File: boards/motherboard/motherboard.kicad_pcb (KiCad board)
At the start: 2 copper layers, 36 parts, among them J1 RJ45, J2 RJ45, J3 RJ45, J4 RJ45, J5 RJ45, U1 EBAYPCA9685

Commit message: mother board pcb
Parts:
- added P1: CONN_01X02, Pin_Headers:Pin_Header_Straight_1x02, F.Cu at (74.9, 133.3)
- added P2: CONN_01X04, Pin_Headers:Pin_Header_Straight_1x04, F.Cu at (59.7, 129.5)
- added P3: CONN_01X04, Pin_Headers:Pin_Header_Straight_1x04, F.Cu at (59.7, 114.3)
- added REF**: MountingHole_2-5mm, Mounting_Holes:MountingHole_2-5mm, F.Cu at (91.4, 134.6)
- 350ma11, 350ma12, 350ma14, 350ma2, 350ma4, 350ma6, 350ma8: moved to B.Cu
- moved R3 146.2 mm to (238.8, 80.0)
- moved U1 139.8 mm to (256.5, 83.8), turned to 270 degrees
- moved J5 137.3 mm to (144.8, 130.8)
- moved R2 132.2 mm to (224.8, 80.0)
- moved R1 118.3 mm to (210.8, 80.0)
- moved J3 105.5 mm to (167.6, 130.8)
- moved R4 104.3 mm to (196.8, 80.0)
- moved 350ma12 97.9 mm to (146.2, 120.7), turned to 180 degrees
- moved R5 90.4 mm to (182.9, 80.0)
- moved 350ma14 89.5 mm to (98.4, 120.7), turned to 180 degrees
- moved 350ma15 77.1 mm to (66.9, 120.7)
- moved R6 76.4 mm to (168.9, 80.0)
- moved J4 68.8 mm to (190.5, 130.8)
- moved R8 62.5 mm to (154.9, 80.0)
- moved 350ma13 62.1 mm to (91.3, 120.7)
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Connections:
- 350ma9 pad 5: +24V -> /led8
- R12 pad 1: VCC -> Net-(R12-Pad1)
- R9 pad 2: +24V -> /led8
- U1 pad 19: Net-(U1-Pad19) -> /sda
- U1 pad 20: Net-(U1-Pad20) -> /scl
- U1 pad 9: +24V -> /led8
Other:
- board outline added: 223.5 x 63.5 mm
- net class 24vpower added: clearance 0.2, trace_width 2, via_dia 0.6, via_drill 0.4
- net class 350power added: clearance 0.2, trace_width 0.4, via_dia 0.6, via_drill 0.4

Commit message: sort of ok
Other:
- outline, holes or cut-outs redrawn
- net class 24vpower: trace_width 2 -> 8
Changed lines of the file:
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@@
   (net_class 24vpower ""
     (clearance 0.2)
-    (trace_width 2)
+    (trace_width 8)
     (via_dia 0.6)
     (via_drill 0.4)
@@
   (gr_line (start 53.34 139.7) (end 53.34 76.2) (angle 90) (layer Edge.Cuts) (width 0.15))
   (gr_line (start 276.86 139.7) (end 53.34 139.7) (angle 90) (layer Edge.Cuts) (width 0.15))
-  (gr_line (start 276.86 77.47) (end 276.86 139.7) (angle 90) (layer Edge.Cuts) (width 0.15))
+  (gr_line (start 276.86 76.2) (end 276.86 139.7) (angle 90) (layer Edge.Cuts) (width 0.15))
   (gr_line (start 276.86 76.2) (end 53.34 76.2) (angle 90) (layer Edge.Cuts) (width 0.15))
 )

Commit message: before autoroute
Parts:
- added REF10: MountingHole_2-5mm, Mounting_Holes:MountingHole_2-5mm, F.Cu at (251.5, 133.3)
- added REF2: MountingHole_2-5mm, Mounting_Holes:MountingHole_2-5mm, F.Cu at (58.7, 103.4)
- added REF3: MountingHole_2-5mm, Mounting_Holes:MountingHole_2-5mm, F.Cu at (251.5, 80.0)
- added REF4: MountingHole_2-5mm, Mounting_Holes:MountingHole_2-5mm, F.Cu at (121.9, 133.3)
- added REF5: MountingHole_2-5mm, Mounting_Holes:MountingHole_2-5mm, F.Cu at (146.1, 133.3)
- added REF6: MountingHole_2-5mm, Mounting_Holes:MountingHole_2-5mm, F.Cu at (168.9, 133.3)
- added REF7: MountingHole_2-5mm, Mounting_Holes:MountingHole_2-5mm, F.Cu at (191.8, 133.3)
- added REF8: MountingHole_2-5mm, Mounting_Holes:MountingHole_2-5mm, F.Cu at (214.6, 133.3)
- added REF9: MountingHole_2-5mm, Mounting_Holes:MountingHole_2-5mm, F.Cu at (237.5, 133.3)
- J1, J2, J3, J4, J5: footprint lighting:RJ45 -> Connect:RJ45_8
- P1: footprint Pin_Headers:Pin_Header_Straight_1x02 -> lighting:TerminalBlock
- moved P2 186.9 mm to (246.4, 138.4)
- moved P3 184.5 mm to (242.6, 138.4)
- moved P1 56.5 mm to (58.7, 79.2), turned to 180 degrees
- moved R14 46.0 mm to (86.4, 115.6)
- moved R1 29.2 mm to (210.8, 109.2)
- moved R10 29.2 mm to (85.1, 109.2)
- moved R11 29.2 mm to (99.1, 109.2)
- moved R12 29.2 mm to (127.0, 109.2)
- moved R13 29.2 mm to (71.1, 109.2)
- moved R2 29.2 mm to (224.8, 109.2)
- moved R3 29.2 mm to (238.8, 109.2)
- moved R4 29.2 mm to (196.8, 109.2)
- moved R5 29.2 mm to (182.9, 109.2)
- moved R6 29.2 mm to (168.9, 109.2)
- moved R7 29.2 mm to (113.0, 109.2)
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- renumbered REF** to REF1
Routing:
- net +24V: track 0.00 -> 355.8 mm
- net GNDPWR: track 0.00 -> 286.9 mm
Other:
- board size 223.5 x 63.5 mm -> 223.5 x 66 mm
- net class 24vpower: trace_width 8 -> 4

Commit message: after route
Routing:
- net VCC: track 0.00 -> 251.6 mm
- net GND: track 0.00 -> 251.5 mm
- net /led14: track 0.00 -> 222.7 mm
- net /led12: track 0.00 -> 203.3 mm
- net /led13: track 0.00 -> 192.5 mm
- net /led9: track 0.00 -> 180.1 mm
- net /led10: track 0.00 -> 166.1 mm
- net /led11: track 0.00 -> 147.3 mm
- net /led6: track 0.00 -> 145.8 mm
- net /led8: track 0.00 -> 128.4 mm
- net /led7: track 0.00 -> 111.8 mm
- net /led5: track 0.00 -> 95.3 mm
- net /led4: track 0.00 -> 95.3 mm
- net Net-(350ma15-Pad3): track 0.00 -> 71.7 mm
- net /led0: track 0.00 -> 69.0 mm
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
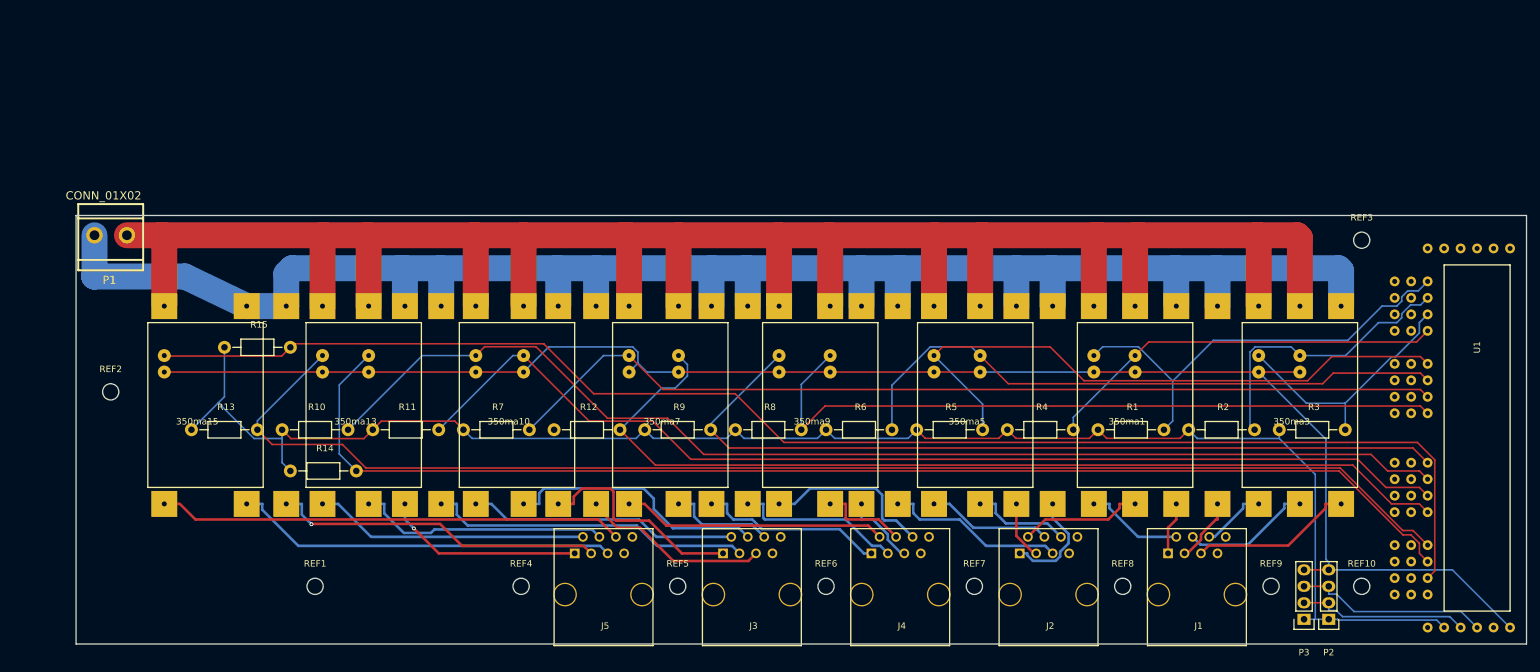
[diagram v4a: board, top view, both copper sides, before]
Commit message: moved parts around and swapped pca footprint
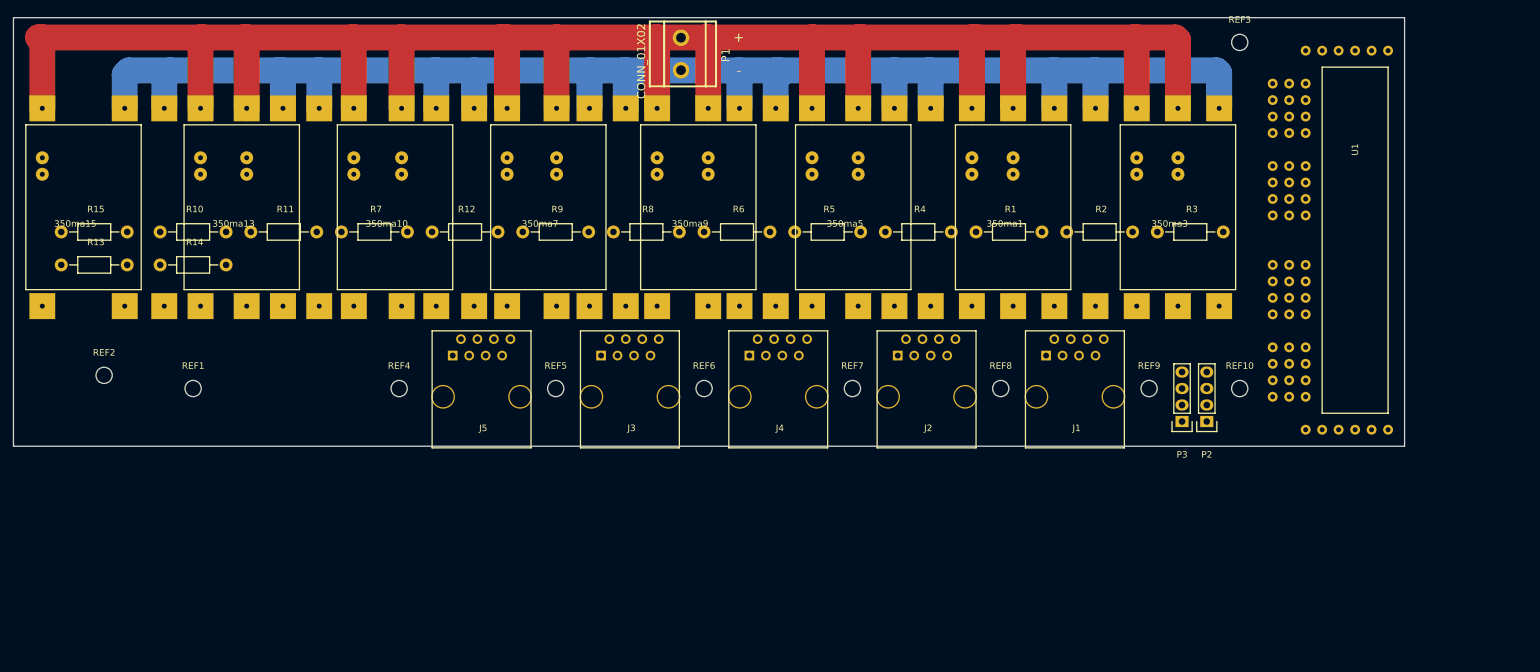
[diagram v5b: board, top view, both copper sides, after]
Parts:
- moved P1 92.2 mm to (146.6, 51.3), turned to 270 degrees
- moved R14 37.6 mm to (66.3, 83.8)
- moved 350ma3 35.8 mm to (216.8, 90.2)
- moved REF3 35.8 mm to (232.7, 49.5)
- moved U1 35.8 mm to (237.7, 55.9)
- moved 350ma10 35.8 mm to (96.1, 90.2)
- moved 350ma11 35.8 mm to (103.5, 90.2)
- moved 350ma13 35.8 mm to (72.5, 90.2)
- moved 350ma15 35.8 mm to (48.1, 90.2)
- moved J5 35.8 mm to (115.8, 104.1)
- moved R10 35.8 mm to (66.3, 78.7)
- moved R11 35.8 mm to (80.3, 78.7)
- moved R12 35.8 mm to (108.2, 78.7)
- moved R7 35.8 mm to (94.2, 78.7)
- moved 350ma1 35.8 mm to (191.4, 90.2)
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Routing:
- net VCC: track 251.6 -> 0.00 mm
- net GND: track 251.5 -> 0.00 mm
- net /led14: track 222.7 -> 0.00 mm
- net /led12: track 203.3 -> 0.00 mm
- net /led13: track 192.5 -> 0.00 mm
- net /led9: track 180.1 -> 0.00 mm
- net /led10: track 166.1 -> 0.00 mm
- net /led11: track 147.3 -> 0.00 mm
- net /led6: track 145.8 -> 0.00 mm
- net /led8: track 128.4 -> 0.00 mm
- net /led7: track 111.8 -> 0.00 mm
- net /led5: track 95.3 -> 0.00 mm
- net /led4: track 95.3 -> 0.00 mm
- net Net-(350ma15-Pad3): track 71.7 -> 0.00 mm
- net /led0: track 69.0 -> 0.00 mm
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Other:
- board size 223.5 x 66 mm -> 214.4 x 66 mm
- board text added: "+"
- board text added: "-"

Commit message: before auto route
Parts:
- moved REF1 51.3 mm to (54.6, 54.4)
- moved REF2 8.87 mm to (66.3, 102.9)
- moved REF3 3.05 mm to (235.7, 49.5)
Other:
- board text added: "This board can take up to 30V and drive 5 20W RGB LEDs. Do not use common anode or common cathode LEDs with this board."
- board text added: "gnd"
- board text added: "sda"
- board text added: "vcc"
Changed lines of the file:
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@@
     (area 43.612999 44.689419 258.139001 114.025)
     (thickness 1.6)
-    (drawings 6)
+    (drawings 13)
     (tracks 117)
     (zones 0)
@@
     (descr "Mounting hole, Befestigungsbohrung, 2,5mm, No Annular, Kein Restring,")
     (tags "Mounting hole, Befestigungsbohrung, 2,5mm, No Annular, Kein Restring,")
-    (fp_text reference REF10 (at 0 -3.50012) (layer F.SilkS)
+    (fp_text reference REF10 (at 0 -3.50012) (layer F.SilkS) hide
       (effects (font (size 1 1) (thickness 0.15)))
     )
@@
     (descr "Mounting hole, Befestigungsbohrung, 2,5mm, No Annular, Kein Restring,")
     (tags "Mounting hole, Befestigungsbohrung, 2,5mm, No Annular, Kein Restring,")
-    (fp_text reference REF9 (at 0 -3.50012) (layer F.SilkS)
+    (fp_text reference REF9 (at 0 -3.50012) (layer F.SilkS) hide
       (effects (font (size 1 1) (thickness 0.15)))
     )
@@
     (descr "Mounting hole, Befestigungsbohrung, 2,5mm, No Annular, Kein Restring,")
     (tags "Mounting hole, Befestigungsbohrung, 2,5mm, No Annular, Kein Restring,")
-    (fp_text reference REF8 (at 0 -3.50012) (layer F.SilkS)
+    (fp_text reference REF8 (at 0 -3.50012) (layer F.SilkS) hide
       (effects (font (size 1 1) (thickness 0.15)))
     )
@@
     (descr "Mounting hole, Befestigungsbohrung, 2,5mm, No Annular, Kein Restring,")
     (tags "Mounting hole, Befestigungsbohrung, 2,5mm, No Annular, Kein Restring,")
-    (fp_text reference REF7 (at 0 -3.50012) (layer F.SilkS)
+    (fp_text reference REF7 (at 0 -3.50012) (layer F.SilkS) hide
       (effects (font (size 1 1) (thickness 0.15)))
     )
@@
     (descr "Mounting hole, Befestigungsbohrung, 2,5mm, No Annular, Kein Restring,")
     (tags "Mounting hole, Befestigungsbohrung, 2,5mm, No Annular, Kein Restring,")
-    (fp_text reference REF6 (at 0 -3.50012) (layer F.SilkS)
+    (fp_text reference REF6 (at 0 -3.50012) (layer F.SilkS) hide
       (effects (font (size 1 1) (thickness 0.15)))
     )
@@
   )
   (module Mounting_Holes:MountingHole_2-5mm (layer F.Cu)
-    (at 232.664 49.53)
+    (at 235.712 49.53)
     (descr "Mounting hole, Befestigungsbohrung, 2,5mm, No Annular, Kein Restring,")
     (tags "Mounting hole, Befestigungsbohrung, 2,5mm, No Annular, Kein Restring,")
@@
   )
   (module Mounting_Holes:MountingHole_2-5mm (layer F.Cu)
-    (at 57.658 100.838)
+    (at 66.294 102.87)
     (descr "Mounting hole, Befestigungsbohrung, 2,5mm, No Annular, Kein Restring,")
     (tags "Mounting hole, Befestigungsbohrung, 2,5mm, No Annular, Kein Restring,")
-    (fp_text reference REF2 (at 0 -3.50012) (layer F.SilkS)
+    (fp_text reference REF2 (at 0 -3.50012) (layer F.SilkS) hide
       (effects (font (size 1 1) (thickness 0.15)))
     )
@@
   )
   (module Mounting_Holes:MountingHole_2-5mm (layer F.Cu)
-    (at 71.374 102.87)
+    (at 54.61 54.356)
     (descr "Mounting hole, Befestigungsbohrung, 2,5mm, No Annular, Kein Restring,")
     (tags "Mounting hole, Befestigungsbohrung, 2,5mm, No Annular, Kein Restring,")
-    (fp_text reference REF1 (at 0 -3.50012) (layer F.SilkS)
+    (fp_text reference REF1 (at 0 -3.50012) (layer F.SilkS) hide
       (effects (font (size 1 1) (thickness 0.15)))
     )
@@
     (descr "Mounting hole, Befestigungsbohrung, 2,5mm, No Annular, Kein Restring,")
     (tags "Mounting hole, Befestigungsbohrung, 2,5mm, No Annular, Kein Restring,")
-    (fp_text reference REF4 (at 0 -3.50012) (layer F.SilkS)
+    (fp_text reference REF4 (at 0 -3.50012) (layer F.SilkS) hide
       (effects (font (size 1 1) (thickness 0.15)))
     )
@@
     (descr "Mounting hole, Befestigungsbohrung, 2,5mm, No Annular, Kein Restring,")
     (tags "Mounting hole, Befestigungsbohrung, 2,5mm, No Annular, Kein Restring,")
-    (fp_text reference REF5 (at 0 -3.50012) (layer F.SilkS)
+    (fp_text reference REF5 (at 0 -3.50012) (layer F.SilkS) hide
       (effects (font (size 1 1) (thickness 0.15)))
     )
@@
     (pad 60 thru_hole circle (at 48.26 0 270) (size 1.524 1.524) (drill 0.762) (layers *.Cu *.Mask F.SilkS))
   )
+  (gr_line (start 230.124 106.172) (end 232.664 106.172) (angle 90) (layer F.SilkS) (width 0.2))
+  (gr_line (start 230.124 105.664) (end 230.124 106.172) (angle 90) (layer F.SilkS) (width 0.2))
+  (gr_line (start 229.108 105.664) (end 230.124 105.664) (angle 90) (layer F.SilkS) (width 0.2))
+  (gr_text sda (at 234.696 106.172) (layer F.SilkS)
+    (effects (font (size 1.5 1.5) (thickness 0.3)))
+  )
+  (gr_text gnd (at 231.648 98.806) (layer F.SilkS)
+    (effects (font (size 1.5 1.5) (thickness 0.3)))
+  )
+  (gr_text "vcc\n" (at 231.648 107.95) (layer F.SilkS)
+    (effects (font (size 1.5 1.5) (thickness 0.3)))
+  )
+  (gr_text "This board can take up to 30V and drive 5 20W RGB \nLEDs. Do not use common anode or common\ncathode LEDs with this board." (at 45.466 96.266) (layer F.SilkS)
+    (effects (font (size 1.5 1.5) (thickness 0.3)) (justify left))
+  )
   (gr_text - (at 155.448 53.848) (layer F.SilkS)

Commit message: after auto route
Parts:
- moved REF1 57.3 mm to (85.1, 102.9)
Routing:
- net VCC: track 0.00 -> 273.6 mm
- net GND: track 0.00 -> 262.7 mm
- net /led14: track 0.00 -> 213.8 mm
- net /led12: track 0.00 -> 194.0 mm
- net /led13: track 0.00 -> 187.3 mm
- net /led9: track 0.00 -> 181.2 mm
- net /led10: track 0.00 -> 163.5 mm
- net /led6: track 0.00 -> 154.4 mm
- net /led11: track 0.00 -> 134.6 mm
- net /led8: track 0.00 -> 119.4 mm
- net /led7: track 0.00 -> 115.2 mm
- net /led5: track 0.00 -> 100.6 mm, vias 0 -> 1
- net /led3: track 0.00 -> 90.1 mm
- net /led4: track 0.00 -> 88.4 mm
- net /led0: track 0.00 -> 77.0 mm
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
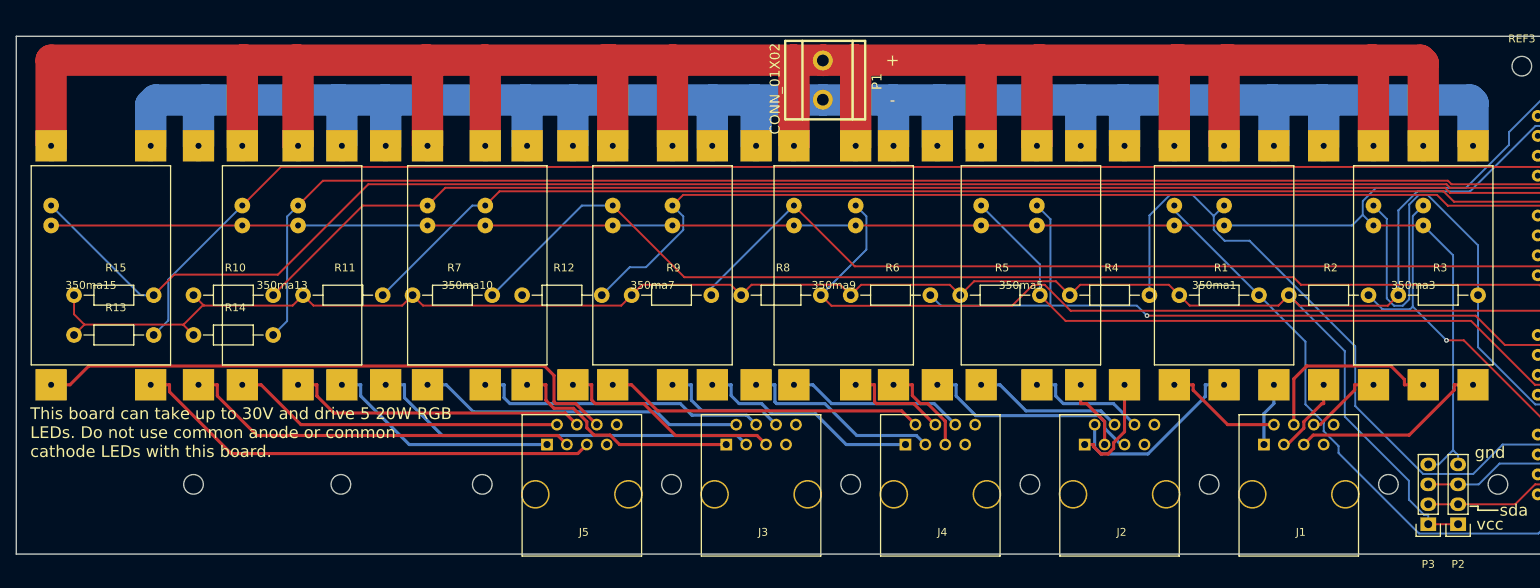
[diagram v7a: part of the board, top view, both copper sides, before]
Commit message: added zones
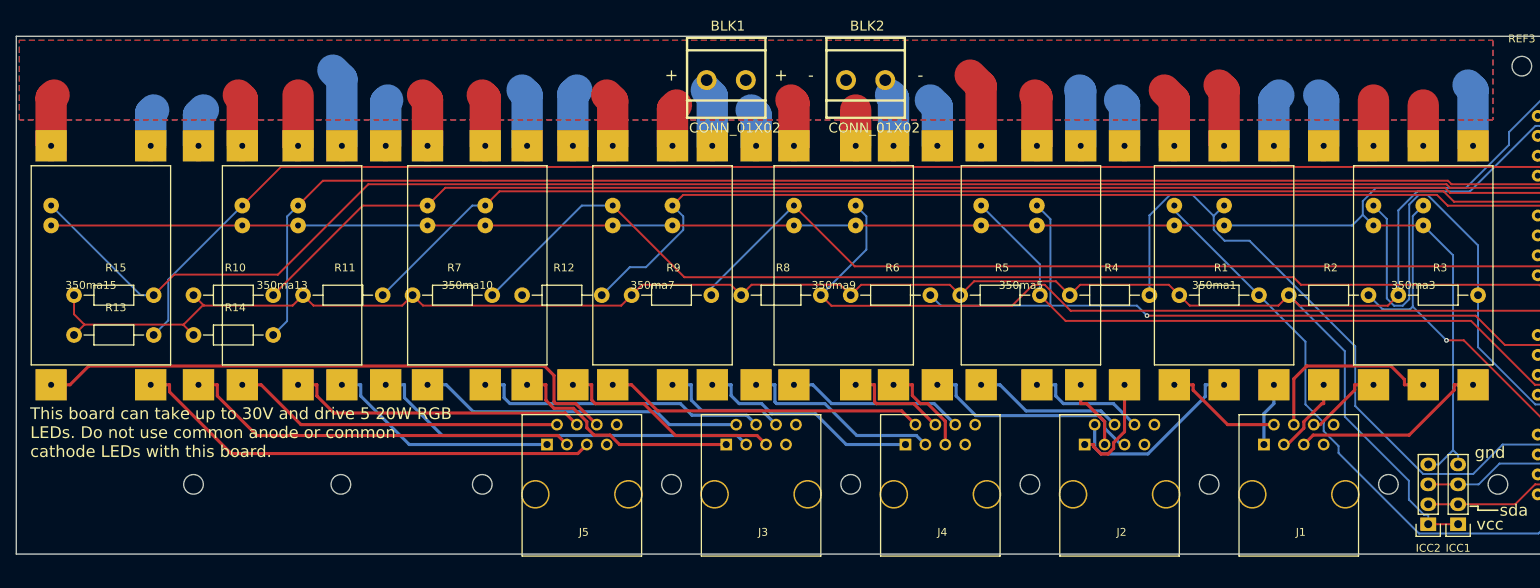
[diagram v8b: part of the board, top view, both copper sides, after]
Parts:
- removed P1: CONN_01X02, lighting:TerminalBlock
- removed P2, P3: CONN_01X04, Pin_Headers:Pin_Header_Straight_1x04
- added BLK1: CONN_01X02, lighting:TerminalBlock, F.Cu at (134.2, 51.3)
- added BLK2: CONN_01X02, lighting:TerminalBlock, F.Cu at (152.0, 51.3)
- added ICC1: CONN_01X04, Pin_Headers:Pin_Header_Straight_1x04, F.Cu at (227.6, 108.0)
- added ICC2: CONN_01X04, Pin_Headers:Pin_Header_Straight_1x04, F.Cu at (223.8, 108.0)
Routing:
- net +24V: track 345.4 -> 98.8 mm
- net GNDPWR: track 261.1 -> 100.2 mm
- added copper zone on F.Cu, net +24V
- added copper zone on B.Cu, net GNDPWR
